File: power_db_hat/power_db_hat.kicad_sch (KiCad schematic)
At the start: 35 parts, among them J2 BAT1, J3 12V_out, J5 24V_out, J6 Conn_01x04_Pin, J8 BAT2

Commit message: lol
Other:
- moved on the sheet: C1, C2, C4, JP2, JP3, JP4, R1, R2, R3, R4

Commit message: UPDATE
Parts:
- D1: value 3V3 -> LED_R
- D2: value 5V -> LED_R
- D3: value 12V -> LED_R
- D4: value 24V -> LED_R
- D5: value LED -> LED_R
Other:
- sheet expansion ports: added none; removed EXP_INT, GPA0, GPA1, GPA2, GPA3, GPA4, GPA5, GPA6, GPA7, I2C_SCL, I2C_SDA, PD_RST
- moved on the sheet: D1, D2, D3, D4, D5, R10, R11, R12, R13, R14

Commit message: lol
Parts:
- removed C30: 100nF, Capacitor_SMD:C_0603_1608Metric_Pad1.08x0.95mm_HandSolder, symbol Device:C
- removed D10: TVS_3V3, Diode_SMD:D_0603_1608Metric_Pad1.05x0.95mm_HandSolder, symbol Device:D_Zener
- removed D11, D9: TVS_13V, Diode_SMD:D_0603_1608Metric_Pad1.05x0.95mm_HandSolder, symbol Device:D_Zener
- removed F2: FUSE_5A, Fuse:Fuse_2512_6332Metric_Pad1.52x3.35mm_HandSolder, symbol Device:Fuse
- removed J3: 12V_out, CONN_AMASS_3D_FIXED:AMASS_XT60PW-F_1x02_P7.20mm_Horizontal, symbol Connector:Conn_01x02_Pin
- removed J6: Conn_01x04_Pin, Connector_JST:JST_SH_SM04B-SRSS-TB_1x04-1MP_P1.00mm_Horizontal, symbol Connector:Conn_01x04_Pin
- removed JP2, JP3: SolderJumper_2_Open, Jumper:SolderJumper-2_P1.3mm_Open_TrianglePad1.0x1.5mm, symbol Jumper:SolderJumper_2_Open
- removed R1, R2, R3, R4: 0, Resistor_SMD:R_0603_1608Metric_Pad0.98x0.95mm_HandSolder, symbol Device:R_US
- added C45, C47, C49: 100nF, Capacitor_SMD:C_0603_1608Metric_Pad1.08x0.95mm_HandSolder, symbol Device:C
- added C46, C48, C50: 22uF, Capacitor_SMD:C_0603_1608Metric_Pad1.08x0.95mm_HandSolder, symbol Device:C
- added J17, J7, J9: Conn_02x06_Counter_Clockwise, Connector_PinSocket_2.54mm:PinSocket_2x06_P2.54mm_Vertical_SMD, symbol Connector_Generic:Conn_02x06_Odd_Even
- added JP6, JP7, JP8: SolderJumper_2_Open, Jumper:SolderJumper-2_P1.3mm_Open_TrianglePad1.0x1.5mm, symbol Jumper:SolderJumper_2_Open
- added TP1, TP2, TP3, TP4: TestPoint, TestPoint:TestPoint_Pad_D1.0mm, symbol Connector:TestPoint
- J2, J8: footprint CONN_AMASS_3D_FIXED:AMASS_XT60PW-M_1x02_P7.20mm_Horizontal -> AMASS_Custom:AMASS_XT60PW-M_1x02_P7.20mm_Horizontal
- J5: footprint CONN_AMASS_3D_FIXED:AMASS_XT60PW-F_1x02_P7.20mm_Horizontal -> AMASS_Custom:AMASS_XT60PW-F_1x02_P7.20mm_Horizontal
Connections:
- net +12V: now also C49.2, C50.1, J17.1 (Pin_1), J17.3 (Pin_3), J17.5 (Pin_5), J17.7 (Pin_7), JP6.1 (A), TP3.1
- net +24V: now also JP8.1 (A), TP4.1
- net +3V3: now also C45.2, C46.1, J17.2 (Pin_2), J17.4 (Pin_4), TP1.1
- net +5V: now also C4.2, C47.2, C48.1, J17.10 (Pin_10), J17.12 (Pin_12), J17.6 (Pin_6), J17.8 (Pin_8), TP2.1
- net GND: now also C45.1, C46.2, C47.1, C48.2, C49.1, C50.2, J17.11 (Pin_11), J17.9 (Pin_9), J7.1 (Pin_1), J7.10 (Pin_10), J7.11 (Pin_11), J7.12 (Pin_12), J7.3 (Pin_3), J7.4 (Pin_4), J7.6 (Pin_6), J7.8 (Pin_8), J9.1 (Pin_1), J9.10 (Pin_10), J9.11 (Pin_11), J9.12 (Pin_12), J9.3 (Pin_3), J9.5 (Pin_5), J9.6 (Pin_6), J9.7 (Pin_7), J9.8 (Pin_8), J9.9 (Pin_9)
- net I2C_SDA: now also J7.2 (Pin_2)
- net VBAT2+: now also JP7.1 (A)
- net power/5V_OUT: no longer C4.2
- net power/VIN_24V: now also JP7.2 (B)
- net power/VOUT_12V: now also JP6.2 (B)
- net power/VOUT_24V: now also JP8.2 (B)
- new net IND_2: J7.5 (Pin_5)
- new net IND_3: J7.7 (Pin_7)
- new net IND_4: J7.9 (Pin_9)
- new net SERVO_1: J9.2 (Pin_2)
- new net SERVO_2: J9.4 (Pin_4)
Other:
- removed sheet HAT_connections
- sheet expansion ports: added LED_PWM_1, LED_PWM_2; removed PWM_3, PWM_4
- sheet power ports: added none; removed BUCK_IN, VIN_12V
- note removed: "PD power"
- moved on the sheet: D39, D40, D41, D8, F1, J2, J5, J8, JP4

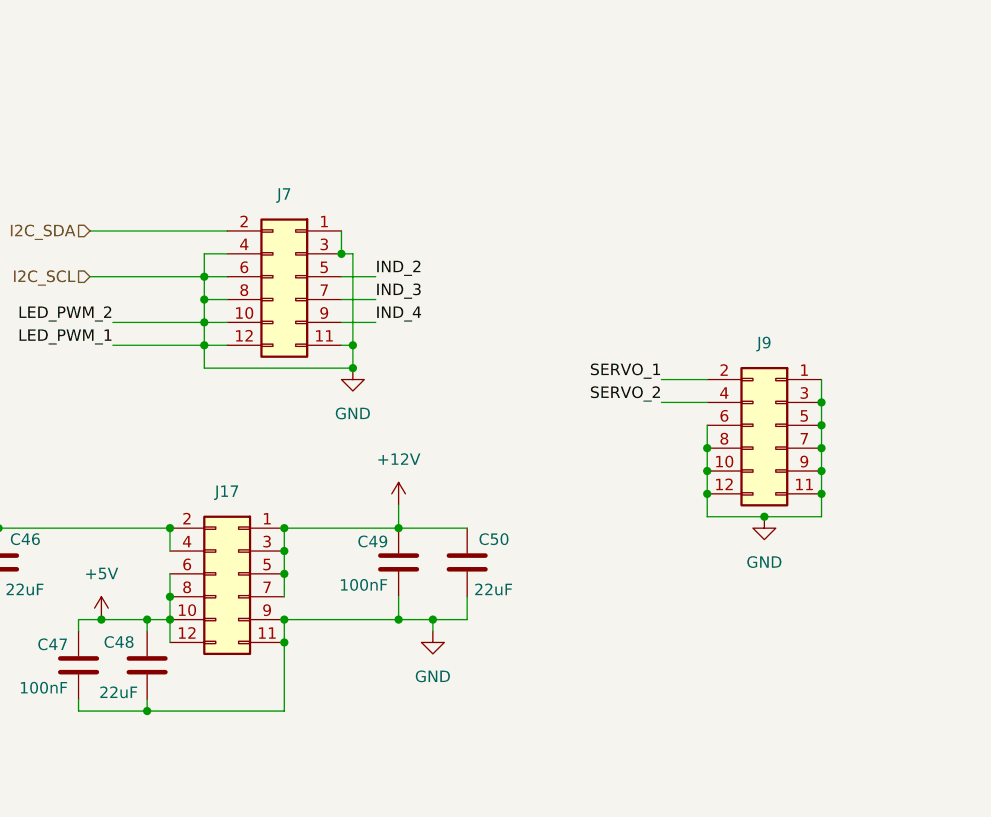
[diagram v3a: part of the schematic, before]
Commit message: made b2b footprint
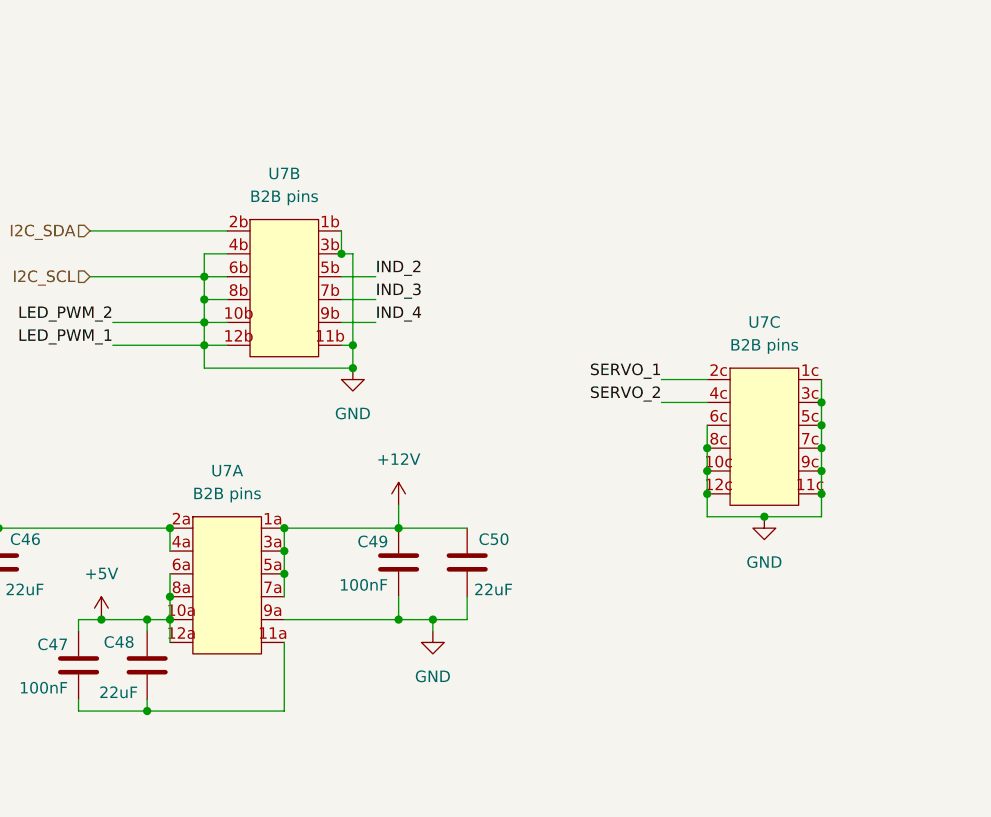
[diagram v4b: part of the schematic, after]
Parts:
- removed J17, J7, J9: Conn_02x06_Counter_Clockwise, Connector_PinSocket_2.54mm:PinSocket_2x06_P2.54mm_Vertical_SMD, symbol Connector_Generic:Conn_02x06_Odd_Even
- added U7: B2B pins, B2B-Connectors:B2B_pin_socket_3x(02x06), symbol B2B-Connectors:B2B_pin_socket
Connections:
- net +12V: now also U7.1a, U7.3a, U7.5a, U7.7a
- net +3V3: now also U7.2a, U7.4a
- net +5V: now also U7.10a, U7.12a, U7.6a, U7.8a
- net GND: now also U7.10b, U7.10c, U7.11b, U7.11c, U7.12b, U7.12c, U7.1b, U7.1c, U7.3b, U7.3c, U7.4b, U7.5c, U7.6b, U7.6c, U7.7c, U7.8b, U7.8c, U7.9a, U7.9c; no longer C47.1, C48.2
- net I2C_SDA: now also U7.2b
- net IND_2: now also U7.5b
- net IND_3: now also U7.7b
- net IND_4: now also U7.9b
- net SERVO_1: now also U7.2c
- net SERVO_2: now also U7.4c
- new net: C47.1, C48.2, U7.11a

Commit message: update
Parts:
- removed D39, D40: TVS_13V, Diode_SMD:D_0603_1608Metric_Pad1.05x0.95mm_HandSolder, symbol Device:D_Zener
- removed D8: TVS_26V, Diode_SMD:D_0603_1608Metric_Pad1.05x0.95mm_HandSolder, symbol Device:D_Zener
- removed JP7, JP8: SolderJumper_2_Open, Jumper:SolderJumper-2_P1.3mm_Open_TrianglePad1.0x1.5mm, symbol Jumper:SolderJumper_2_Open
- added D10: TVS_26V, Diode_SMD:D_SMB_Handsoldering, symbol Device:D_TVS
- added D8, D9: TVS_13V, Diode_SMD:D_SMB_Handsoldering, symbol Device:D_TVS
- J2: value BAT1 -> BAT2
- J8: value BAT2 -> BAT1
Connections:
- net IND_2 is gone; now on net +5V: U7.5b
- net IND_3 is gone; now on net +5V: U7.7b
- net IND_4 is gone; now on net +3V3: U7.9b
- net +12V: now also U7.11a, U7.9a; no longer U7.1a, U7.3a
- net +24V: now also D10.2 (A2); no longer F1.2
- net +3V3: now also U7.11b; no longer U7.2a, U7.4a
- net +5V: now also U7.1b, U7.2b, U7.3b, U7.4b; no longer U7.10a, U7.12a, U7.6a, U7.8a
- net GND: now also C47.1, C48.2, U7.10a, U7.12a, U7.1a, U7.2a, U7.3a, U7.4a, U7.6a, U7.8a, D10.1 (A1), D9.1 (A1); no longer U7.11b, U7.11c, U7.12b, U7.1b, U7.1c, U7.3b, U7.3c, U7.4b, U7.5c, U7.7c, U7.8b, U7.9a, U7.9c
- net I2C_SDA: now also U7.8b; no longer U7.2b
- net VBAT1+: now also D8.1 (A1), D9.2 (A2)
- net VBAT2+: now also F1.1, D8.2 (A2); no longer D41.1 (K)
- new net I2C_SCL: U7.12b
- new net LED_PWM_1: U7.9c
- new net LED_PWM_2: U7.11c
- new net MOTOR_1_A: U7.1c
- new net MOTOR_1_B: U7.3c
- new net MOTOR_2_A: U7.5c
- new net MOTOR_2_B: U7.7c
- new net VBAT_24V: D41.1 (K), F1.2
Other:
- sheet expansion ports: added MOTOR_1_A, MOTOR_1_B, MOTOR_2_A, MOTOR_2_B; removed none
- moved on the sheet: C45, C46, C47, C48, C49, C50, D41, F1

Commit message: lol
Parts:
- removed JP4, JP6: SolderJumper_2_Open, Jumper:SolderJumper-2_P1.3mm_Open_TrianglePad1.0x1.5mm, symbol Jumper:SolderJumper_2_Open
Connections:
- net +3V3: now also U7.8c; no longer U7.11b, U7.9b
- net +5V: now also U7.10b, U7.12b, U7.6b, U7.8b; no longer U7.1b, U7.2b, U7.7b
- net GND: now also U7.1b, U7.2b, U7.9b; no longer U7.10b, U7.6b, U7.6c, U7.8c
- net I2C_SCL: now also U7.7b; no longer U7.12b
- net I2C_SDA: now also U7.11b; no longer U7.8b
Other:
- moved on the sheet: C47, C48

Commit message: LMAO
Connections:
- net +5V: now also U7.1b, U7.2b, U7.7b; no longer U7.10b, U7.12b
- net GND: now also U7.10b; no longer U7.1b, U7.2b
- net I2C_SCL: now also U7.12b; no longer U7.7b
